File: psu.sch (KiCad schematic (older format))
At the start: 5 parts, among them U501 LM2576xx

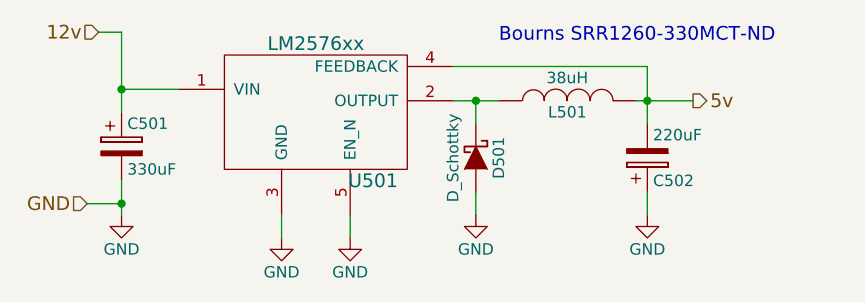
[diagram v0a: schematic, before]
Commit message: Rework most of board for rusefi
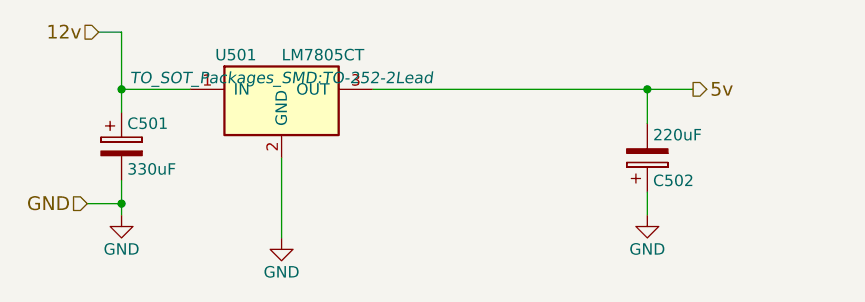
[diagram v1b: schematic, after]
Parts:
- removed D501: D_Schottky, Diodes_SMD:SMC_Standard, symbol D_Schottky
- removed L501: 38uH, Choke_SMD:Choke_SMD_12x12mm_h6mm, symbol INDUCTOR
- removed U501: LM2576xx, TO_SOT_Packages_SMD:TO-263-5Lead, symbol LM2576xx
- added U501: LM7805CT, TO_SOT_Packages_SMD:TO-252-2Lead, symbol LM7805CT
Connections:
- net 12v: now also U501.1 (IN)
- net 5v: now also U501.3 (OUT)
- net GND: now also U501.2 (GND)
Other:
- note removed: "Bourns SRR1260-330MCT-ND"
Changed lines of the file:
@@
 $EndDescr
 $Comp
-L GND #PWR0107
+L GND #PWR0115
 U 1 1 5854D39D
 P 2700 3100
-F 0 "#PWR0107" H 2700 2850 50  0001 C CNN
+F 0 "#PWR0115" H 2700 2850 50  0001 C CNN
 F 1 "GND" H 2700 2950 50  0000 C CNN
 F 2 "" H 2700 3100 50  0000 C CNN
@@
 $EndComp
 $Comp
-L GND #PWR0108
-U 1 1 5854D3A3
-P 3550 3000
-F 0 "#PWR0108" H 3550 2750 50  0001 C CNN
-F 1 "GND" H 3550 2850 50  0000 C CNN
-F 2 "" H 3550 3000 50  0000 C CNN
-F 3 "" H 3550 3000 50  0000 C CNN
-	1    3550 3000
-	1    0    0    -1
-$EndComp
-$Comp
-L GND #PWR0109
+L GND #PWR0116
 U 1 1 5854D3A9
 P 2000 3000
-F 0 "#PWR0109" H 2000 2750 50  0001 C CNN
+F 0 "#PWR0116" H 2000 2750 50  0001 C CNN
 F 1 "GND" H 2000 2850 50  0000 C CNN
 F 2 "" H 2000 3000 50  0000 C CNN
@@
 	1    0    0    -1
 $EndComp
-$Comp
-L LM2576xx U501
-U 1 1 5854D3BB
-P 2850 2600
-F 0 "U501" H 3100 2350 60  0000 C CNN
-F 1 "LM2576xx" H 2850 2950 60  0000 C CNN
-F 2 "TO_SOT_Packages_SMD:TO-263-5Lead" H 2650 3050 60  0001 C CNN
-F 3 "" H 2650 3050 60  0001 C CNN
-	1    2850 2600
-	1    0    0    -1
-$EndComp
-$Comp
-L GND #PWR0110
-U 1 1 5854D3C2
-P 3000 3100
-F 0 "#PWR0110" H 3000 2850 50  0001 C CNN
-F 1 "GND" H 3000 2950 50  0000 C CNN
-F 2 "" H 3000 3100 50  0000 C CNN
-F 3 "" H 3000 3100 50  0000 C CNN
-	1    3000 3100
-	1    0    0    -1
-$EndComp
-Wire Wire Line
-	3000 3100 3000 3000
-Wire Wire Line
-	2700 3000 2700 3100
 $Comp
 L CP C501
@@
 	1    0    0    -1
 $EndComp
-$Comp
-L INDUCTOR L501
-U 1 1 5854D3DB
-P 3950 2500
-F 0 "L501" V 3900 2500 50  0000 C CNN
-F 1 "38uH" V 4050 2500 50  0000 C CNN
-F 2 "Choke_SMD:Choke_SMD_12x12mm_h6mm" H 3950 2500 50  0001 C CNN
-F 3 "" H 3950 2500 50  0000 C CNN
-	1    3950 2500
-	0    -1   -1   0
-$EndComp
 Wire Wire Line
 	2000 2200 2000 2550
 Wire Wire Line
-	2000 2450 2250 2450
-Connection ~ 2000 2450
-Wire Wire Line
 	2000 2850 2000 3000
-$Comp
-L D_Schottky D501
-U 1 1 5854D3E6
-P 3550 2750
-F 0 "D501" H 3550 2850 50  0000 C CNN
-F 1 "D_Schottky" H 3550 2650 50  0000 C CNN
-F 2 "Diodes_SMD:SMC_Standard" H 3550 2750 50  0001 C CNN
-F 3 "" H 3550 2750 50  0000 C CNN
-	1    3550 2750
-	0    1    1    0
-$EndComp
-Wire Wire Line
-	3550 3000 3550 2900
-Wire Wire Line
-	3550 2600 3550 2500
-Wire Wire Line
-	3450 2500 3650 2500
-Connection ~ 3550 2500
-Wire Wire Line
-	4300 2350 4300 2600
-Wire Wire Line
-	4300 2350 3450 2350
 $Comp
 L CP C502
@@
 	1    0    0    1
 $EndComp
-Wire Wire Line
-	4250 2500 4500 2500
-Connection ~ 4300 2500
 $Comp
-L GND #PWR0111
+L GND #PWR0117
 U 1 1 5854D403
 P 4300 3000
-F 0 "#PWR0111" H 4300 2750 50  0001 C CNN
+F 0 "#PWR0117" H 4300 2750 50  0001 C CNN
 F 1 "GND" H 4300 2850 50  0000 C CNN
 F 2 "" H 4300 3000 50  0000 C CNN
@@
 Wire Wire Line
 	4300 2900 4300 3000
-Text Notes 3650 2250 0    60   ~ 0
-Bourns SRR1260-330MCT-ND
-Text HLabel 4500 2500 2    60   Output ~ 0
+Text HLabel 4500 2450 2    60   Output ~ 0
 5v
 Text HLabel 1900 2200 0    60   Input ~ 0
@@
 Wire Wire Line
 	1900 2200 2000 2200
+Wire Wire Line
+	4300 2600 4300 2450
+Connection ~ 4300 2450
+Connection ~ 2000 2450
+Wire Wire Line
+	2700 2750 2700 3100
+$Comp
+L LM7805CT U501
+U 1 1 588C8181
+P 2700 2500
+F 0 "U501" H 2500 2700 50  0000 C CNN
+F 1 "LM7805CT" H 2700 2700 50  0000 L CNN
+F 2 "TO_SOT_Packages_SMD:TO-252-2Lead" H 2700 2600 50  0000 C CIN
+F 3 "" H 2700 2500 50  0000 C CNN
+	1    2700 2500
+	1    0    0    -1
+$EndComp
+Wire Wire Line
+	2300 2450 2000 2450
+Wire Wire Line
+	3100 2450 4500 2450
 $EndSCHEMATC

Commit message: start redoing layout, lowside drivers and analog routed
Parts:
- C501: footprint Capacitors_SMD:c_elec_10x10 -> Capacitors_SMD:CP_Elec_10x10
- C502: footprint Capacitors_Tantalum_SMD:Tantalum_Case-D_EIA-7343-31_Hand -> Capacitors_Tantalum_SMD:CP_Tantalum_Case-D_EIA-7343-31_Hand
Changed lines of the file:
@@
 $EndDescr
 $Comp
-L GND #PWR502
+L GND #PWR0123
 U 1 1 5854D39D
 P 2700 3100
-F 0 "#PWR502" H 2700 2850 50  0001 C CNN
+F 0 "#PWR0123" H 2700 2850 50  0001 C CNN
 F 1 "GND" H 2700 2950 50  0000 C CNN
 F 2 "" H 2700 3100 50  0000 C CNN
@@
 $EndComp
 $Comp
-L GND #PWR501
+L GND #PWR0124
 U 1 1 5854D3A9
 P 2000 3000
-F 0 "#PWR501" H 2000 2750 50  0001 C CNN
+F 0 "#PWR0124" H 2000 2750 50  0001 C CNN
 F 1 "GND" H 2000 2850 50  0000 C CNN
 F 2 "" H 2000 3000 50  0000 C CNN
@@
 F 0 "C501" H 2025 2800 50  0000 L CNN
 F 1 "330uF" H 2025 2600 50  0000 L CNN
-F 2 "Capacitors_SMD:c_elec_10x10" H 2038 2550 50  0001 C CNN
+F 2 "Capacitors_SMD:CP_Elec_10x10" H 2038 2550 50  0001 C CNN
 F 3 "" H 2000 2700 50  0000 C CNN
 	1    2000 2700
@@
 F 0 "C502" H 4325 2850 50  0000 L CNN
 F 1 "220uF" H 4325 2650 50  0000 L CNN
-F 2 "Capacitors_Tantalum_SMD:Tantalum_Case-D_EIA-7343-31_Hand" H 4338 2600 50  0001 C CNN
+F 2 "Capacitors_Tantalum_SMD:CP_Tantalum_Case-D_EIA-7343-31_Hand" H 4338 2600 50  0001 C CNN
 F 3 "" H 4300 2750 50  0000 C CNN
 	1    4300 2750
@@
 $EndComp
 $Comp
-L GND #PWR503
+L GND #PWR0125
 U 1 1 5854D403
 P 4300 3000
-F 0 "#PWR503" H 4300 2750 50  0001 C CNN
+F 0 "#PWR0125" H 4300 2750 50  0001 C CNN
 F 1 "GND" H 4300 2850 50  0000 C CNN
 F 2 "" H 4300 3000 50  0000 C CNN
